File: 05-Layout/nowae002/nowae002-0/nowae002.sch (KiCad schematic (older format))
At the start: 24 parts

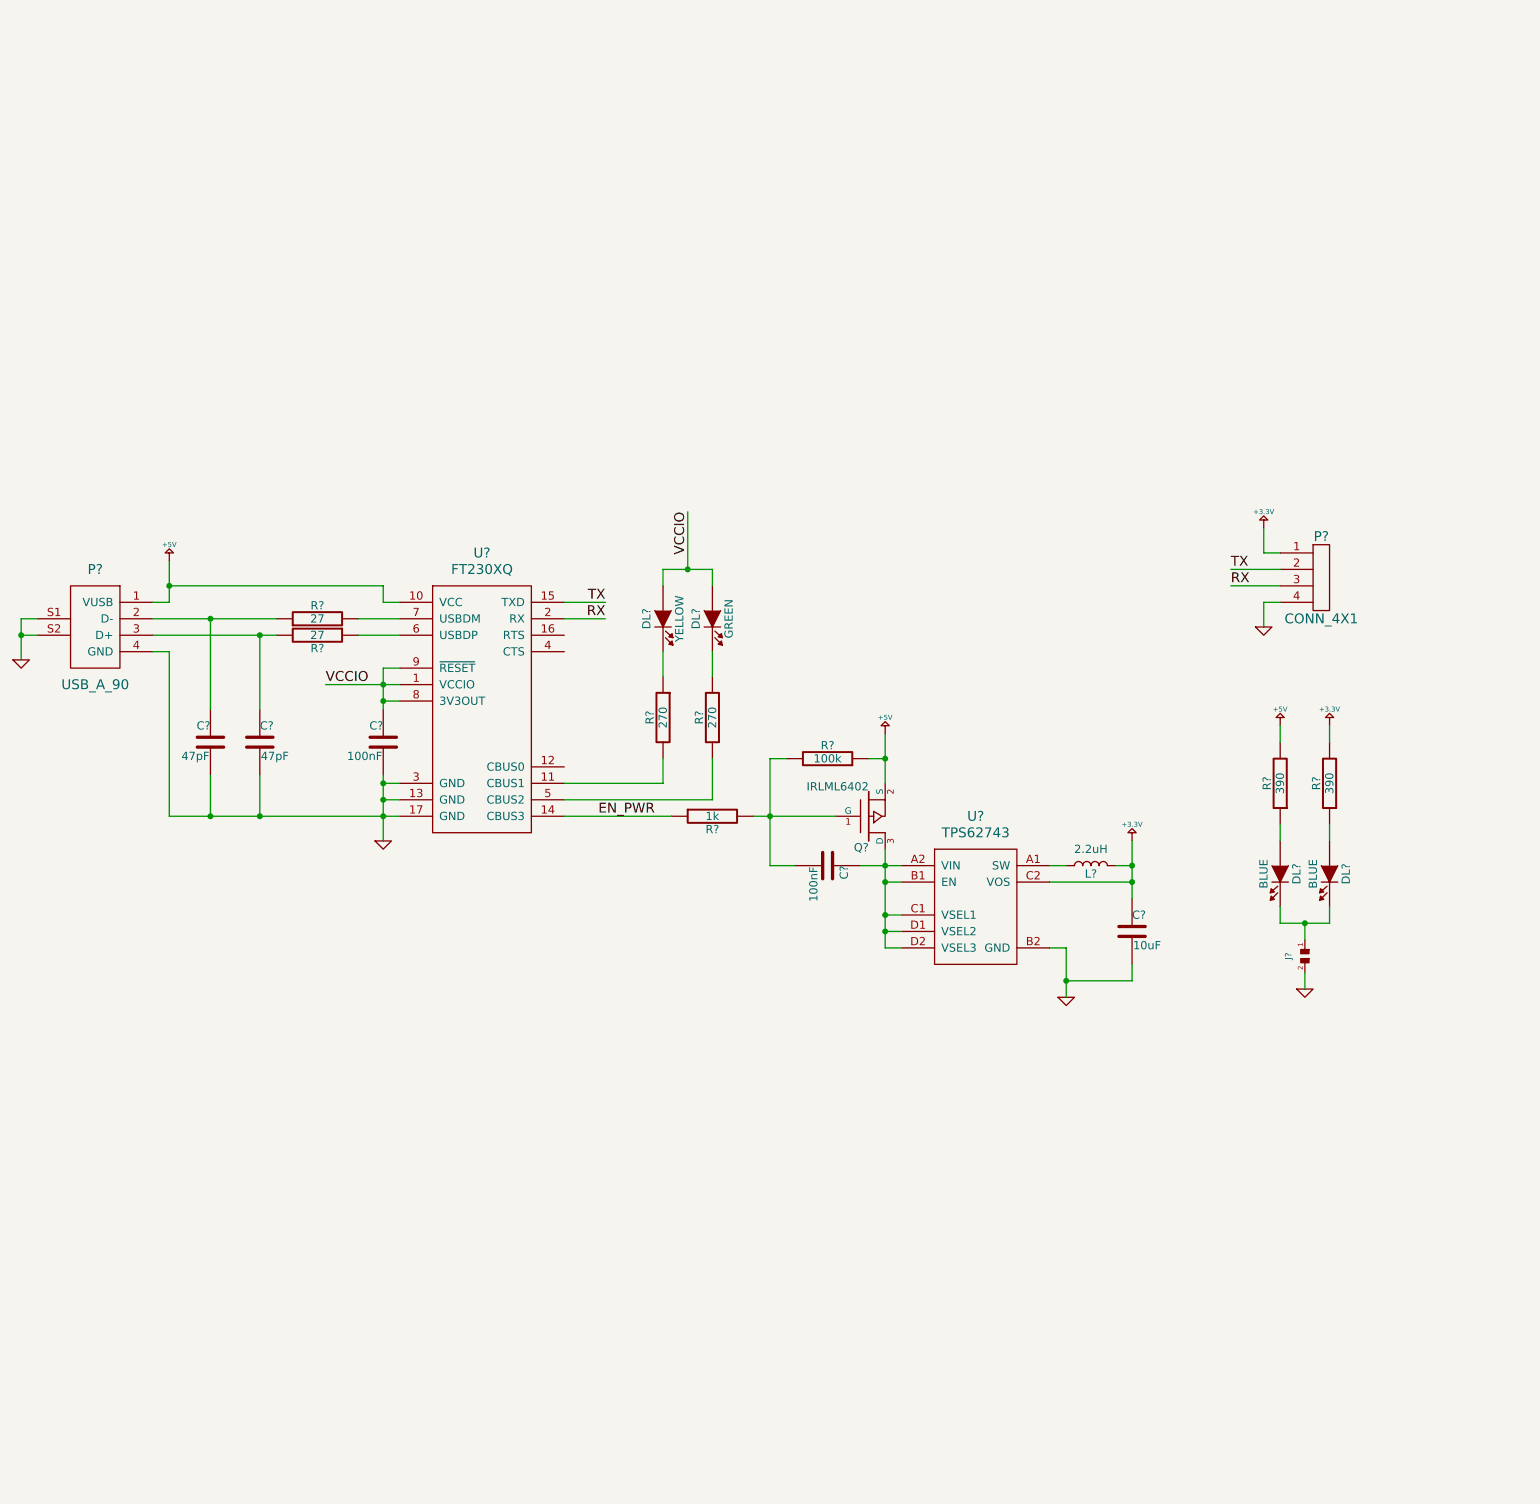
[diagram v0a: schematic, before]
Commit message: Added leds for bluetooth module signals
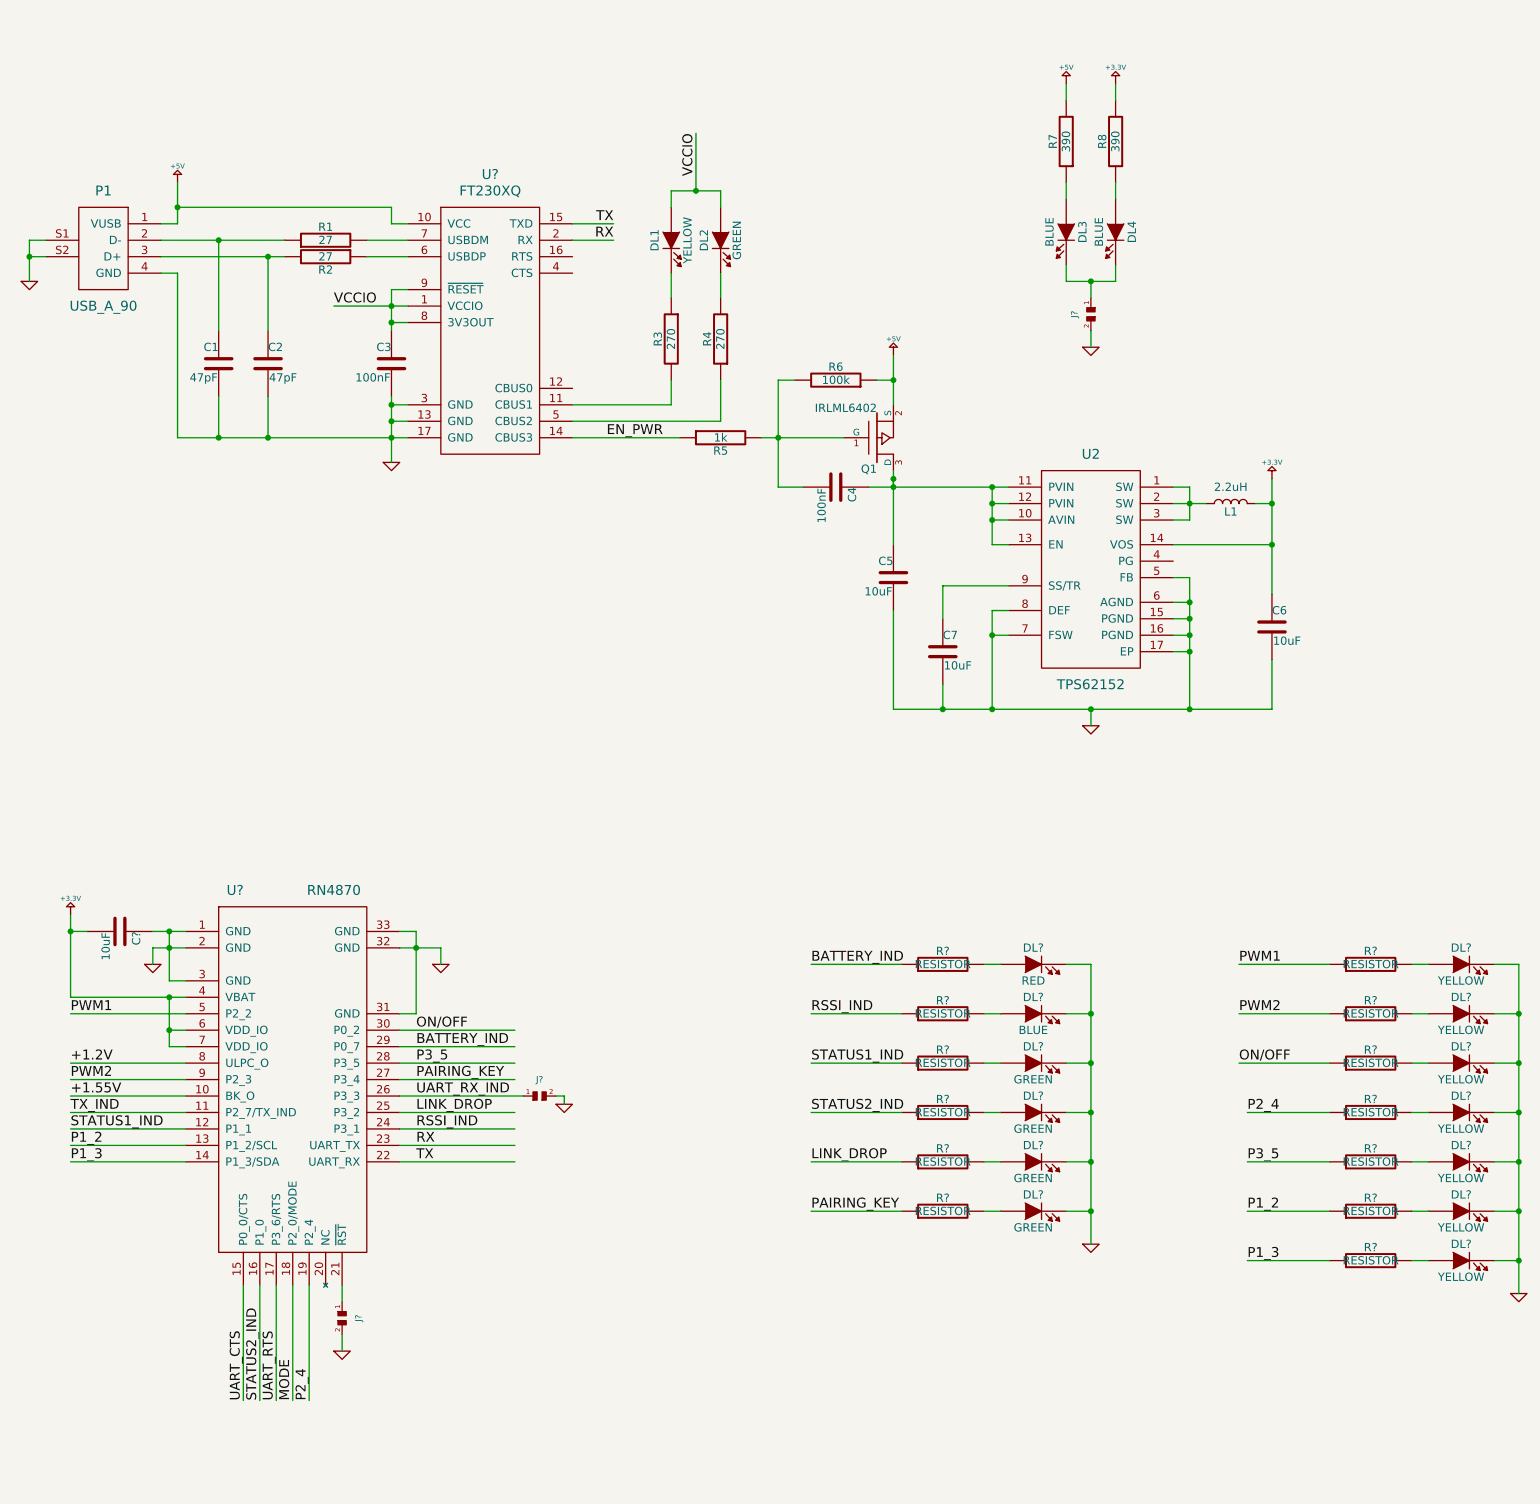
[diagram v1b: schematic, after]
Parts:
- removed P?: CONN_4X1, symbol CONN_4X1
- removed Q?: IRLML6402, symbol IRLML6402
- removed U?: TPS62743, DSBGA8, symbol TPS62743
- added C5, C7, C?: 10uF, symbol CAPACITOR
- added DL?: RED, symbol RED
- added DL? (x7): YELLOW, symbol YELLOW
- added DL? (x4): GREEN, symbol GREEN
- added DL?: BLUE, symbol BLUE
- added J? (x2): SMALL_JUMPER, symbol SMALL_JUMPER
- added Q1: IRLML6402, symbol IRLML6402
- added R? (x13): RESISTOR, symbol RESISTOR
- added U2: TPS62152, VQFN16, symbol TPS62152
- added U?: RN4870, symbol RN4870
- gave numbers to parts that had none: 19
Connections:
- net labels added: +1.2V, +1.55V, BATTERY_IND, LINK_DROP, MODE, ON/OFF, P1_2, P1_3, P2_4, P3_5, PAIRING_KEY, PWM1, PWM2, RSSI_IND, STATUS1_IND, STATUS2_IND, TX_IND, UART_CTS, UART_RTS, UART_RX_IND
- wire segments 100 -> 167
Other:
- moved on the sheet: C1, C2, C3, C4, C6, DL1, DL2, DL3, DL4, J?, L1, P1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

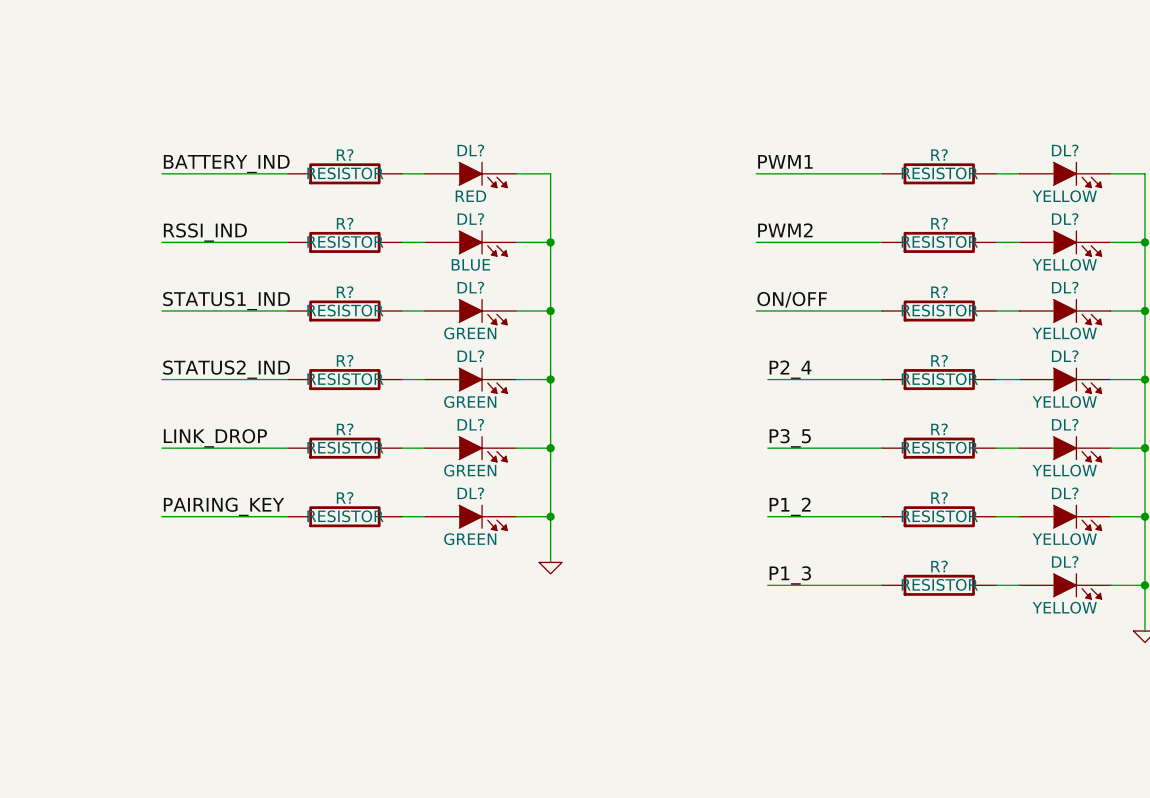
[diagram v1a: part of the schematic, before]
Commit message: Defined led resistors in nowae002
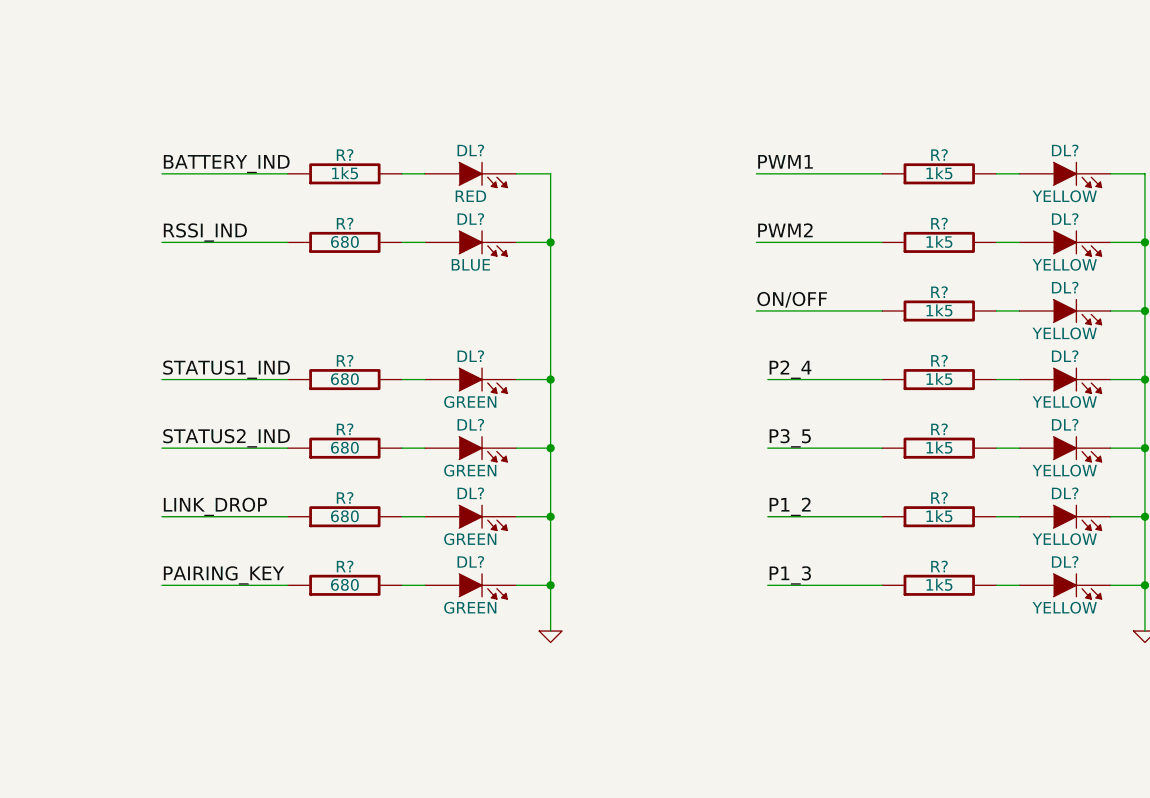
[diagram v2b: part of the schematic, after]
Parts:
- R? (x8): value RESISTOR -> 1k5
- R? (x5): value RESISTOR -> 680
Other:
- moved on the sheet: DL?, R?
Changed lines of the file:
@@
 P 9250 6950
 F 0 "R?" V 9330 6950 50  0000 C CNN
-F 1 "RESISTOR" V 9250 6950 50  0000 C CNN
+F 1 "1k5" V 9250 6950 50  0000 C CNN
 F 2 "" V 9180 6950 30  0001 C CNN
 F 3 "" H 9250 6950 30  0001 C CNN
@@
 L GREEN DL?
 U 1 1 58D55719
-P 9800 7550
-F 0 "DL?" H 9800 7650 50  0000 C CNN
-F 1 "GREEN" H 9800 7450 50  0000 C CNN
-F 2 "" H 9800 7550 60  0001 C CNN
-F 3 "Green" H 9800 7550 60  0001 C CNN
-	1    9800 7550
+P 9800 7850
+F 0 "DL?" H 9800 7950 50  0000 C CNN
+F 1 "GREEN" H 9800 7750 50  0000 C CNN
+F 2 "" H 9800 7850 60  0001 C CNN
+F 3 "Green" H 9800 7850 60  0001 C CNN
+	1    9800 7850
 	1    0    0    -1
 $EndComp
@@
 P 11850 7550
 F 0 "R?" V 11930 7550 50  0000 C CNN
-F 1 "RESISTOR" V 11850 7550 50  0000 C CNN
+F 1 "1k5" V 11850 7550 50  0000 C CNN
 F 2 "" V 11780 7550 30  0001 C CNN
 F 3 "" H 11850 7550 30  0001 C CNN
@@
 P 9250 7250
 F 0 "R?" V 9330 7250 50  0000 C CNN
-F 1 "RESISTOR" V 9250 7250 50  0000 C CNN
+F 1 "680" V 9250 7250 50  0000 C CNN
 F 2 "" V 9180 7250 30  0001 C CNN
 F 3 "" H 9250 7250 30  0001 C CNN
@@
 P 11850 7250
 F 0 "R?" V 11930 7250 50  0000 C CNN
-F 1 "RESISTOR" V 11850 7250 50  0000 C CNN
+F 1 "1k5" V 11850 7250 50  0000 C CNN
 F 2 "" V 11780 7250 30  0001 C CNN
 F 3 "" H 11850 7250 30  0001 C CNN
@@
 P 11850 6950
 F 0 "R?" V 11930 6950 50  0000 C CNN
-F 1 "RESISTOR" V 11850 6950 50  0000 C CNN
+F 1 "1k5" V 11850 6950 50  0000 C CNN
 F 2 "" V 11780 6950 30  0001 C CNN
 F 3 "" H 11850 6950 30  0001 C CNN
@@
 L RESISTOR R?
 U 1 1 58D5827E
-P 9250 7550
-F 0 "R?" V 9330 7550 50  0000 C CNN
-F 1 "RESISTOR" V 9250 7550 50  0000 C CNN
-F 2 "" V 9180 7550 30  0001 C CNN
-F 3 "" H 9250 7550 30  0001 C CNN
-	1    9250 7550
-	0    -1   -1   0
-$EndComp
-$Comp
-L RESISTOR R?
-U 1 1 58D5831A
 P 9250 7850
 F 0 "R?" V 9330 7850 50  0000 C CNN
-F 1 "RESISTOR" V 9250 7850 50  0000 C CNN
+F 1 "680" V 9250 7850 50  0000 C CNN
 F 2 "" V 9180 7850 30  0001 C CNN
 F 3 "" H 9250 7850 30  0001 C CNN
@@
 $EndComp
 $Comp
+L RESISTOR R?
+U 1 1 58D5831A
+P 9250 8150
+F 0 "R?" V 9330 8150 50  0000 C CNN
+F 1 "680" V 9250 8150 50  0000 C CNN
+F 2 "" V 9180 8150 30  0001 C CNN
+F 3 "" H 9250 8150 30  0001 C CNN
+	1    9250 8150
+	0    -1   -1   0
+$EndComp
+$Comp
 L GREEN DL?
 U 1 1 58D583C0
-P 9800 7850
-F 0 "DL?" H 9800 7950 50  0000 C CNN
-F 1 "GREEN" H 9800 7750 50  0000 C CNN
-F 2 "" H 9800 7850 60  0001 C CNN
-F 3 "Green" H 9800 7850 60  0001 C CNN
-	1    9800 7850
-	1    0    0    -1
-$EndComp
-$Comp
-L GREEN DL?
-U 1 1 58D584B8
 P 9800 8150
 F 0 "DL?" H 9800 8250 50  0000 C CNN
@@
 $EndComp
 $Comp
+L GREEN DL?
+U 1 1 58D584B8
+P 9800 8450
+F 0 "DL?" H 9800 8550 50  0000 C CNN
+F 1 "GREEN" H 9800 8350 50  0000 C CNN
+F 2 "" H 9800 8450 60  0001 C CNN
+F 3 "Green" H 9800 8450 60  0001 C CNN
+	1    9800 8450
+	1    0    0    -1
+$EndComp
+$Comp
 L RESISTOR R?
 U 1 1 58D58554
-P 9250 8150
-F 0 "R?" V 9330 8150 50  0000 C CNN
-F 1 "RESISTOR" V 9250 8150 50  0000 C CNN
-F 2 "" V 9180 8150 30  0001 C CNN
-F 3 "" H 9250 8150 30  0001 C CNN
-	1    9250 8150
-	0    -1   -1   0
-$EndComp
-Wire Wire Line
-	8450 7550 9000 7550
+P 9250 8450
+F 0 "R?" V 9330 8450 50  0000 C CNN
+F 1 "680" V 9250 8450 50  0000 C CNN
+F 2 "" V 9180 8450 30  0001 C CNN
+F 3 "" H 9250 8450 30  0001 C CNN
+	1    9250 8450
+	0    -1   -1   0
+$EndComp
 Wire Wire Line
 	8450 7850 9000 7850
-Text Label 8450 7550 0    60   ~ 0
+Wire Wire Line
+	8450 8150 9000 8150
+Text Label 8450 7850 0    60   ~ 0
 STATUS1_IND
-Text Label 8450 7850 0    60   ~ 0
+Text Label 8450 8150 0    60   ~ 0
 STATUS2_IND
 Text Label 5400 9600 1    60   ~ 0
@@
 Text Label 11100 8750 0    60   ~ 0
 P1_3
-Text Label 8450 8150 0    60   ~ 0
+Text Label 8450 8450 0    60   ~ 0
 LINK_DROP
-Text Label 8450 8450 0    60   ~ 0
+Text Label 8450 8750 0    60   ~ 0
 PAIRING_KEY
 $Comp
 L GREEN DL?
 U 1 1 58E548DA
-P 9800 8450
-F 0 "DL?" H 9800 8550 50  0000 C CNN
-F 1 "GREEN" H 9800 8350 50  0000 C CNN
-F 2 "" H 9800 8450 60  0001 C CNN
-F 3 "Green" H 9800 8450 60  0001 C CNN
-	1    9800 8450
+P 9800 8750
+F 0 "DL?" H 9800 8850 50  0000 C CNN
+F 1 "GREEN" H 9800 8650 50  0000 C CNN
+F 2 "" H 9800 8750 60  0001 C CNN
+F 3 "Green" H 9800 8750 60  0001 C CNN
+	1    9800 8750
 	1    0    0    -1
 $EndComp
@@
 L RESISTOR R?
 U 1 1 58E548E0
-P 9250 8450
-F 0 "R?" V 9330 8450 50  0000 C CNN
-F 1 "RESISTOR" V 9250 8450 50  0000 C CNN
-F 2 "" V 9180 8450 30  0001 C CNN
-F 3 "" H 9250 8450 30  0001 C CNN
-	1    9250 8450
-	0    -1   -1   0
-$EndComp
-Wire Wire Line
-	8450 8150 9000 8150
+P 9250 8750
+F 0 "R?" V 9330 8750 50  0000 C CNN
+F 1 "680" V 9250 8750 50  0000 C CNN
+F 2 "" V 9180 8750 30  0001 C CNN
+F 3 "" H 9250 8750 30  0001 C CNN
+	1    9250 8750
+	0    -1   -1   0
+$EndComp
 Wire Wire Line
 	8450 8450 9000 8450
+Wire Wire Line
+	8450 8750 9000 8750
 $Comp
 L RESISTOR R?
@@
 P 11850 7850
 F 0 "R?" V 11930 7850 50  0000 C CNN
-F 1 "RESISTOR" V 11850 7850 50  0000 C CNN
+F 1 "1k5" V 11850 7850 50  0000 C CNN
 F 2 "" V 11780 7850 30  0001 C CNN
 F 3 "" H 11850 7850 30  0001 C CNN
@@
 P 11850 8150
 F 0 "R?" V 11930 8150 50  0000 C CNN
-F 1 "RESISTOR" V 11850 8150 50  0000 C CNN
+F 1 "1k5" V 11850 8150 50  0000 C CNN
 F 2 "" V 11780 8150 30  0001 C CNN
 F 3 "" H 11850 8150 30  0001 C CNN
@@
 P 11850 8450
 F 0 "R?" V 11930 8450 50  0000 C CNN
-F 1 "RESISTOR" V 11850 8450 50  0000 C CNN
+F 1 "1k5" V 11850 8450 50  0000 C CNN
 F 2 "" V 11780 8450 30  0001 C CNN
 F 3 "" H 11850 8450 30  0001 C CNN
@@
 P 11850 8750
 F 0 "R?" V 11930 8750 50  0000 C CNN
-F 1 "RESISTOR" V 11850 8750 50  0000 C CNN
+F 1 "1k5" V 11850 8750 50  0000 C CNN
 F 2 "" V 11780 8750 30  0001 C CNN
 F 3 "" H 11850 8750 30  0001 C CNN
@@
 	12100 7250 12200 7250
 Wire Wire Line
-	9500 7550 9600 7550
-Wire Wire Line
 	9500 7850 9600 7850
 Wire Wire Line
@@
 Wire Wire Line
 	9500 8450 9600 8450
+Wire Wire Line
+	9500 8750 9600 8750
 Wire Wire Line
 	9500 6950 9600 6950
@@
 L GND #PWR?
 U 1 1 58E58545
-P 10150 8650
-F 0 "#PWR?" H 10150 8650 30  0001 C CNN
-F 1 "GND" H 10150 8650 30  0001 C CNN
-F 2 "" H 10150 8650 60  0000 C CNN
-F 3 "" H 10150 8650 60  0000 C CNN
-	1    10150 8650
-	1    0    0    -1
-$EndComp
+P 10150 8950
+F 0 "#PWR?" H 10150 8950 30  0001 C CNN
+F 1 "GND" H 10150 8950 30  0001 C CNN
+F 2 "" H 10150 8950 60  0000 C CNN
+F 3 "" H 10150 8950 60  0000 C CNN
+	1    10150 8950
+	1    0    0    -1
+$EndComp
+Wire Wire Line
+	10000 8750 10150 8750
+Wire Wire Line
+	10150 6950 10150 8950
 Wire Wire Line
 	10000 8450 10150 8450
-Wire Wire Line
-	10150 6950 10150 8650
+Connection ~ 10150 8750
 Wire Wire Line
 	10000 8150 10150 8150
@@
 Connection ~ 10150 8150
 Wire Wire Line
-	10000 7550 10150 7550
+	10000 7250 10150 7250
 Connection ~ 10150 7850
 Wire Wire Line
-	10000 7250 10150 7250
-Connection ~ 10150 7550
-Wire Wire Line
 	10000 6950 10150 6950
